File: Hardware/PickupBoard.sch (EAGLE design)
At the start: 29 parts, among them U1 TL074_

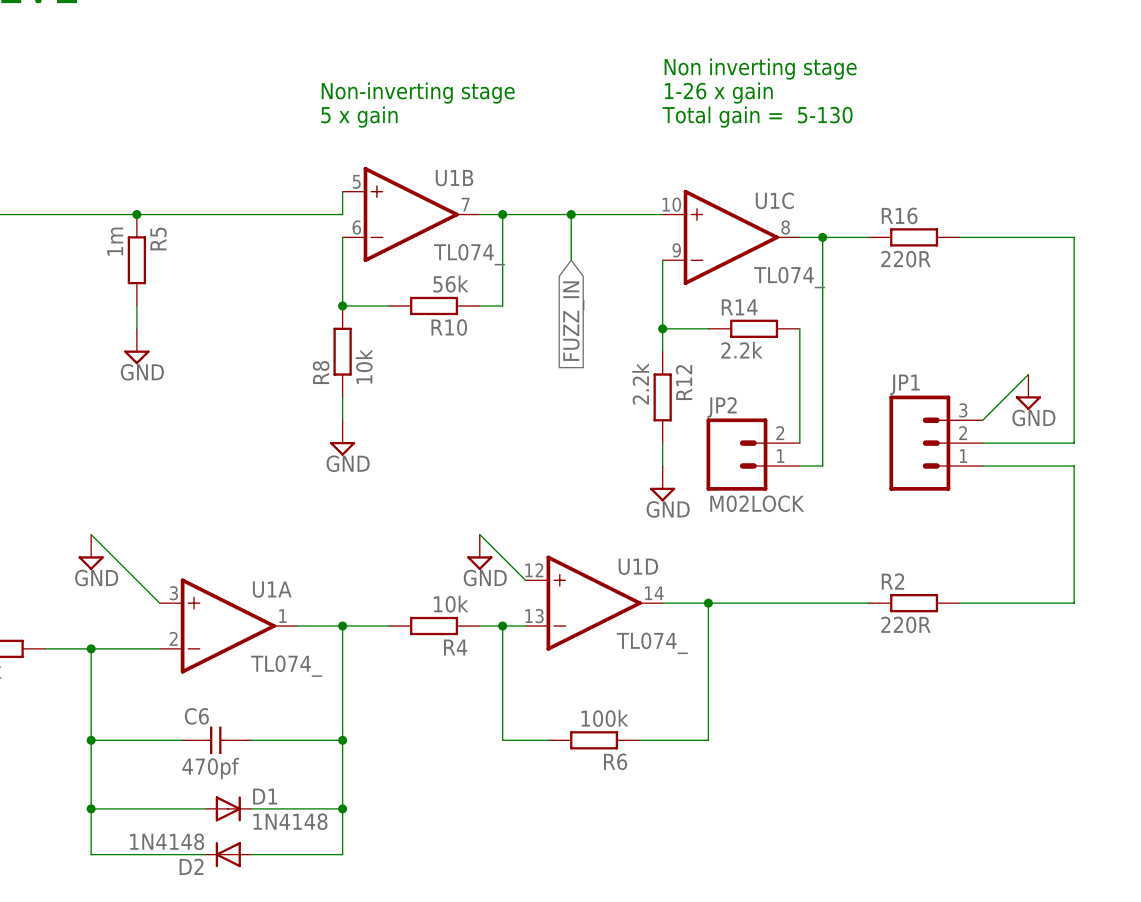
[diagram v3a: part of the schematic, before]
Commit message: Reworked layout to reduce noise / feedback
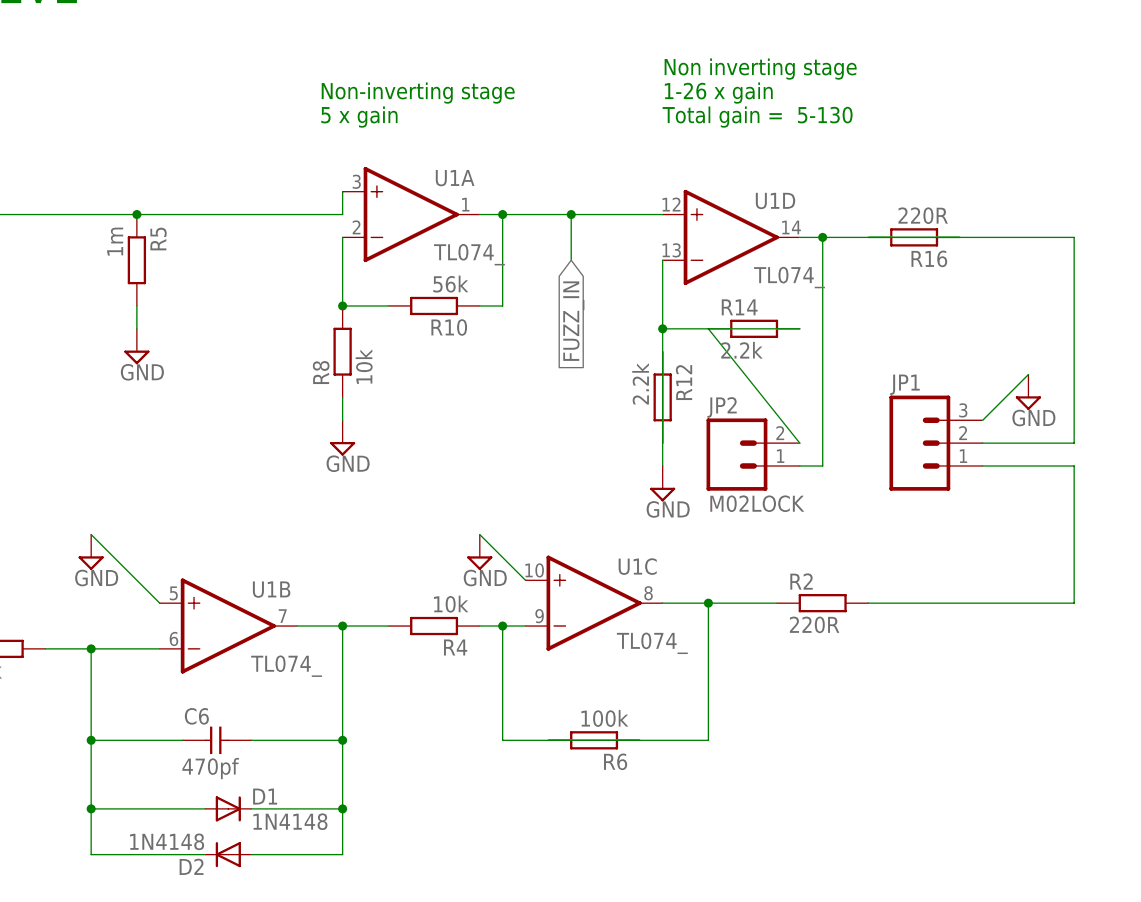
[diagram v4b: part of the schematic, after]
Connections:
- net FUZZ_IN: now also U1A.OUT, U1D.+IN; no longer U1B.OUT, U1C.+IN
- net GND: now also R12.1, U1B.+IN, U1C.+IN; no longer R12.2, U1A.+IN, U1D.+IN
- net N$1: now also U1A.+IN; no longer U1B.+IN
- net N$11: now also R6.2, U1C.OUT; no longer R6.1, U1D.OUT
- net N$2: now also U1B.OUT; no longer U1A.OUT
- net N$3: now also U1A.-IN; no longer U1B.-IN
- net N$4: now also U1B.-IN; no longer U1A.-IN
- net N$5: now also R14.1; no longer R14.2
- net N$6: now also R12.2, R14.2, U1D.-IN; no longer R12.1, R14.1, U1C.-IN
- net N$8: now also U1D.OUT; no longer U1C.OUT
- net N$9: now also R6.1, U1C.-IN; no longer R6.2, U1D.-IN
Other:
- moved on the sheet: R16, R2, U1A, U1B, U1C, U1D
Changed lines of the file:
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@@
 <?xml version="1.0" encoding="utf-8"?>
 <!DOCTYPE eagle SYSTEM "eagle.dtd">
-<eagle version="7.2.0">
+<eagle version="7.4.0">
 <drawing>
 <settings>
@@
 </plain>
 <instances>
-<instance part="U1" gate="B" x="129.54" y="127"/>
-<instance part="U1" gate="C" x="165.1" y="124.46"/>
+<instance part="U1" gate="A" x="129.54" y="127"/>
+<instance part="U1" gate="D" x="165.1" y="124.46"/>
 <instance part="R5" gate="G$1" x="99.06" y="121.92" rot="R270"/>
 <instance part="SUPPLY4" gate="GND" x="99.06" y="111.76"/>
 <instance part="R14" gate="G$1" x="167.64" y="114.3"/>
-<instance part="R16" gate="G$1" x="185.42" y="124.46"/>
+<instance part="R16" gate="G$1" x="185.42" y="124.46" rot="R180"/>
 <instance part="R8" gate="G$1" x="121.92" y="111.76" rot="R90"/>
 <instance part="R10" gate="G$1" x="132.08" y="116.84" rot="R180"/>
@@
 <instance part="FRAME1" gate="G$1" x="0" y="0"/>
 <instance part="C3" gate="G$1" x="66.04" y="78.74" rot="R270"/>
-<instance part="U1" gate="A" x="109.22" y="81.28"/>
+<instance part="U1" gate="B" x="109.22" y="81.28"/>
 <instance part="U1" gate="P" x="104.14" y="27.94"/>
-<instance part="R2" gate="G$1" x="185.42" y="83.82"/>
+<instance part="R2" gate="G$1" x="175.26" y="83.82"/>
 <instance part="U$1" gate="G$1" x="66.04" y="119.38"/>
 <instance part="U$2" gate="G$1" x="38.1" y="25.4"/>
-<instance part="U1" gate="D" x="149.86" y="83.82"/>
+<instance part="U1" gate="C" x="149.86" y="83.82"/>
 <instance part="JP1" gate="G$1" x="185.42" y="101.6"/>
 <instance part="JP2" gate="G$1" x="165.1" y="99.06"/>
@@
 </segment>
 <segment>
-<pinref part="R12" gate="G$1" pin="2"/>
+<pinref part="R12" gate="G$1" pin="1"/>
 <pinref part="SUPPLY5" gate="GND" pin="GND"/>
-<wire x1="157.48" y1="101.6" x2="157.48" y2="99.06" width="0.1524" layer="91"/>
+<wire x1="157.48" y1="111.76" x2="157.48" y2="99.06" width="0.1524" layer="91"/>
 </segment>
 <segment>
@@
 </segment>
 <segment>
-<pinref part="U1" gate="A" pin="+IN"/>
+<pinref part="U1" gate="B" pin="+IN"/>
 <pinref part="SUPPLY1" gate="GND" pin="GND"/>
 <wire x1="93.98" y1="91.44" x2="101.6" y2="83.82" width="0.1524" layer="91"/>
 </segment>
 <segment>
-<pinref part="U1" gate="D" pin="+IN"/>
+<pinref part="U1" gate="C" pin="+IN"/>
 <pinref part="SUPPLY2" gate="GND" pin="GND"/>
 <wire x1="137.16" y1="91.44" x2="142.24" y2="86.36" width="0.1524" layer="91"/>
@@
 <net name="N$8" class="0">
 <segment>
-<pinref part="U1" gate="C" pin="OUT"/>
-<wire x1="180.34" y1="124.46" x2="175.26" y2="124.46" width="0.1524" layer="91"/>
+<pinref part="U1" gate="D" pin="OUT"/>
+<wire x1="190.5" y1="124.46" x2="175.26" y2="124.46" width="0.1524" layer="91"/>
 <wire x1="175.26" y1="124.46" x2="172.72" y2="124.46" width="0.1524" layer="91"/>
 <pinref part="R16" gate="G$1" pin="1"/>
@@
 <segment>
 <pinref part="R16" gate="G$1" pin="2"/>
-<wire x1="203.2" y1="124.46" x2="190.5" y2="124.46" width="0.1524" layer="91"/>
+<wire x1="203.2" y1="124.46" x2="180.34" y2="124.46" width="0.1524" layer="91"/>
 <wire x1="203.2" y1="124.46" x2="203.2" y2="101.6" width="0.1524" layer="91"/>
 <pinref part="JP1" gate="G$1" pin="2"/>
@@
 <pinref part="R8" gate="G$1" pin="2"/>
 <wire x1="127" y1="116.84" x2="121.92" y2="116.84" width="0.1524" layer="91"/>
-<pinref part="U1" gate="B" pin="-IN"/>
+<pinref part="U1" gate="A" pin="-IN"/>
 <wire x1="121.92" y1="116.84" x2="121.92" y2="124.46" width="0.1524" layer="91"/>
 <junction x="121.92" y="116.84"/>
@@
 <net name="N$6" class="0">
 <segment>
-<pinref part="U1" gate="C" pin="-IN"/>
+<pinref part="U1" gate="D" pin="-IN"/>
 <wire x1="157.48" y1="121.92" x2="157.48" y2="114.3" width="0.1524" layer="91"/>
-<pinref part="R12" gate="G$1" pin="1"/>
-<pinref part="R14" gate="G$1" pin="1"/>
-<wire x1="157.48" y1="114.3" x2="157.48" y2="111.76" width="0.1524" layer="91"/>
-<wire x1="162.56" y1="114.3" x2="157.48" y2="114.3" width="0.1524" layer="91"/>
+<pinref part="R12" gate="G$1" pin="2"/>
+<pinref part="R14" gate="G$1" pin="2"/>
+<wire x1="157.48" y1="114.3" x2="157.48" y2="101.6" width="0.1524" layer="91"/>
+<wire x1="172.72" y1="114.3" x2="157.48" y2="114.3" width="0.1524" layer="91"/>
 <junction x="157.48" y="114.3"/>
 </segment>
@@
 <net name="N$5" class="0">
 <segment>
-<pinref part="R14" gate="G$1" pin="2"/>
-<wire x1="172.72" y1="114.3" x2="172.72" y2="101.6" width="0.1524" layer="91"/>
+<pinref part="R14" gate="G$1" pin="1"/>
+<wire x1="162.56" y1="114.3" x2="172.72" y2="101.6" width="0.1524" layer="91"/>
 <pinref part="JP2" gate="G$1" pin="2"/>
 </segment>
@@
 </segment>
 <segment>
-<pinref part="U1" gate="B" pin="OUT"/>
+<pinref part="U1" gate="A" pin="OUT"/>
 <wire x1="137.16" y1="127" x2="139.7" y2="127" width="0.1524" layer="91"/>
 <wire x1="139.7" y1="127" x2="139.7" y2="116.84" width="0.1524" layer="91"/>
@@
 <pinref part="R10" gate="G$1" pin="1"/>
 <wire x1="137.16" y1="116.84" x2="139.7" y2="116.84" width="0.1524" layer="91"/>
-<pinref part="U1" gate="C" pin="+IN"/>
+<pinref part="U1" gate="D" pin="+IN"/>
 <wire x1="139.7" y1="127" x2="147.32" y2="127" width="0.1524" layer="91"/>
 <wire x1="147.32" y1="127" x2="157.48" y2="127" width="0.1524" layer="91"/>
@@
 <wire x1="193.04" y1="99.06" x2="203.2" y2="99.06" width="0.1524" layer="91"/>
 <wire x1="203.2" y1="99.06" x2="203.2" y2="83.82" width="0.1524" layer="91"/>
-<wire x1="203.2" y1="83.82" x2="190.5" y2="83.82" width="0.1524" layer="91"/>
+<wire x1="203.2" y1="83.82" x2="180.34" y2="83.82" width="0.1524" layer="91"/>
 </segment>
 </net>
@@
 <pinref part="R5" gate="G$1" pin="1"/>
 <wire x1="58.42" y1="127" x2="99.06" y2="127" width="0.1524" layer="91"/>
-<pinref part="U1" gate="B" pin="+IN"/>
+<pinref part="U1" gate="A" pin="+IN"/>
 <wire x1="99.06" y1="127" x2="121.92" y2="127" width="0.1524" layer="91"/>
 <wire x1="121.92" y1="127" x2="121.92" y2="129.54" width="0.1524" layer="91"/>
@@
 <net name="N$4" class="0">
 <segment>
-<pinref part="U1" gate="A" pin="-IN"/>
+<pinref part="U1" gate="B" pin="-IN"/>
 <pinref part="R1" gate="G$1" pin="2"/>
 <wire x1="88.9" y1="78.74" x2="93.98" y2="78.74" width="0.1524" layer="91"/>
@@
 <net name="N$2" class="0">
 <segment>
-<pinref part="U1" gate="A" pin="OUT"/>
+<pinref part="U1" gate="B" pin="OUT"/>
 <wire x1="116.84" y1="81.28" x2="121.92" y2="81.28" width="0.1524" layer="91"/>
 <pinref part="D1" gate="G$1" pin="C"/>
@@
 <segment>
 <pinref part="R4" gate="G$1" pin="1"/>
-<pinref part="U1" gate="D" pin="-IN"/>
+<pinref part="U1" gate="C" pin="-IN"/>
 <wire x1="142.24" y1="81.28" x2="139.7" y2="81.28" width="0.1524" layer="91"/>
-<pinref part="R6" gate="G$1" pin="2"/>
+<pinref part="R6" gate="G$1" pin="1"/>
 <wire x1="139.7" y1="81.28" x2="137.16" y2="81.28" width="0.1524" layer="91"/>
-<wire x1="144.78" y1="68.58" x2="139.7" y2="68.58" width="0.1524" layer="91"/>
+<wire x1="154.94" y1="68.58" x2="139.7" y2="68.58" width="0.1524" layer="91"/>
 <wire x1="139.7" y1="68.58" x2="139.7" y2="81.28" width="0.1524" layer="91"/>
 <junction x="139.7" y="81.28"/>
@@
 <net name="N$11" class="0">
 <segment>
-<pinref part="U1" gate="D" pin="OUT"/>
+<pinref part="U1" gate="C" pin="OUT"/>
 <pinref part="R2" gate="G$1" pin="1"/>
-<wire x1="180.34" y1="83.82" x2="162.56" y2="83.82" width="0.1524" layer="91"/>
-<pinref part="R6" gate="G$1" pin="1"/>
+<wire x1="170.18" y1="83.82" x2="162.56" y2="83.82" width="0.1524" layer="91"/>
+<pinref part="R6" gate="G$1" pin="2"/>
 <wire x1="162.56" y1="83.82" x2="157.48" y2="83.82" width="0.1524" layer="91"/>
-<wire x1="154.94" y1="68.58" x2="162.56" y2="68.58" width="0.1524" layer="91"/>
+<wire x1="144.78" y1="68.58" x2="162.56" y2="68.58" width="0.1524" layer="91"/>
 <wire x1="162.56" y1="68.58" x2="162.56" y2="83.82" width="0.1524" layer="91"/>
 <junction x="162.56" y="83.82"/>

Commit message: Rev 4 pcb
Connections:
- net N$2: now also C6.2; no longer C6.1
- net N$4: now also C6.1; no longer C6.2
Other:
- moved on the sheet: C6, R12, R14, R16, R6
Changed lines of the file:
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@@
 <?xml version="1.0" encoding="utf-8"?>
 <!DOCTYPE eagle SYSTEM "eagle.dtd">
-<eagle version="7.4.0">
+<eagle version="7.2.0">
 <drawing>
 <settings>
@@
 <instance part="R5" gate="G$1" x="99.06" y="121.92" rot="R270"/>
 <instance part="SUPPLY4" gate="GND" x="99.06" y="111.76"/>
-<instance part="R14" gate="G$1" x="167.64" y="114.3"/>
-<instance part="R16" gate="G$1" x="185.42" y="124.46" rot="R180"/>
+<instance part="R14" gate="G$1" x="167.64" y="114.3" rot="R180"/>
+<instance part="R16" gate="G$1" x="185.42" y="124.46"/>
 <instance part="R8" gate="G$1" x="121.92" y="111.76" rot="R90"/>
 <instance part="R10" gate="G$1" x="132.08" y="116.84" rot="R180"/>
 <instance part="SUPPLY9" gate="GND" x="121.92" y="101.6"/>
-<instance part="R12" gate="G$1" x="157.48" y="106.68" rot="R270"/>
+<instance part="R12" gate="G$1" x="157.48" y="106.68" rot="R90"/>
 <instance part="SUPPLY5" gate="GND" x="157.48" y="96.52"/>
 <instance part="GND21" gate="1" x="76.2" y="27.94"/>
@@
 <instance part="D1" gate="G$1" x="109.22" y="60.96"/>
 <instance part="D2" gate="G$1" x="109.22" y="55.88" rot="R180"/>
-<instance part="C6" gate="G$1" x="109.22" y="68.58" rot="R270"/>
+<instance part="C6" gate="G$1" x="109.22" y="68.58" rot="R90"/>
 <instance part="R4" gate="G$1" x="132.08" y="81.28" rot="R180"/>
 <instance part="SUPPLY2" gate="GND" x="137.16" y="88.9"/>
-<instance part="R6" gate="G$1" x="149.86" y="68.58" rot="R180"/>
+<instance part="R6" gate="G$1" x="149.86" y="68.58"/>
 </instances>
 <busses>
@@
 <pinref part="R12" gate="G$1" pin="1"/>
 <pinref part="SUPPLY5" gate="GND" pin="GND"/>
-<wire x1="157.48" y1="111.76" x2="157.48" y2="99.06" width="0.1524" layer="91"/>
+<wire x1="157.48" y1="101.6" x2="157.48" y2="99.06" width="0.1524" layer="91"/>
 </segment>
 <segment>
@@
 <segment>
 <pinref part="U1" gate="D" pin="OUT"/>
-<wire x1="190.5" y1="124.46" x2="175.26" y2="124.46" width="0.1524" layer="91"/>
+<wire x1="180.34" y1="124.46" x2="175.26" y2="124.46" width="0.1524" layer="91"/>
 <wire x1="175.26" y1="124.46" x2="172.72" y2="124.46" width="0.1524" layer="91"/>
 <pinref part="R16" gate="G$1" pin="1"/>
@@
 <segment>
 <pinref part="R16" gate="G$1" pin="2"/>
-<wire x1="203.2" y1="124.46" x2="180.34" y2="124.46" width="0.1524" layer="91"/>
+<wire x1="203.2" y1="124.46" x2="190.5" y2="124.46" width="0.1524" layer="91"/>
 <wire x1="203.2" y1="124.46" x2="203.2" y2="101.6" width="0.1524" layer="91"/>
 <pinref part="JP1" gate="G$1" pin="2"/>
@@
 <pinref part="R12" gate="G$1" pin="2"/>
 <pinref part="R14" gate="G$1" pin="2"/>
-<wire x1="157.48" y1="114.3" x2="157.48" y2="101.6" width="0.1524" layer="91"/>
-<wire x1="172.72" y1="114.3" x2="157.48" y2="114.3" width="0.1524" layer="91"/>
+<wire x1="157.48" y1="114.3" x2="157.48" y2="111.76" width="0.1524" layer="91"/>
+<wire x1="162.56" y1="114.3" x2="157.48" y2="114.3" width="0.1524" layer="91"/>
 <junction x="157.48" y="114.3"/>
 </segment>
@@
 <segment>
 <pinref part="R14" gate="G$1" pin="1"/>
-<wire x1="162.56" y1="114.3" x2="172.72" y2="101.6" width="0.1524" layer="91"/>
+<wire x1="172.72" y1="114.3" x2="172.72" y2="101.6" width="0.1524" layer="91"/>
 <pinref part="JP2" gate="G$1" pin="2"/>
 </segment>
@@
 <wire x1="93.98" y1="55.88" x2="93.98" y2="60.96" width="0.1524" layer="91"/>
 <junction x="93.98" y="60.96"/>
-<pinref part="C6" gate="G$1" pin="2"/>
-<wire x1="104.14" y1="68.58" x2="93.98" y2="68.58" width="0.1524" layer="91"/>
+<pinref part="C6" gate="G$1" pin="1"/>
+<wire x1="106.68" y1="68.58" x2="93.98" y2="68.58" width="0.1524" layer="91"/>
 <junction x="93.98" y="68.58"/>
 </segment>
@@
 <wire x1="121.92" y1="55.88" x2="121.92" y2="60.96" width="0.1524" layer="91"/>
 <junction x="121.92" y="60.96"/>
-<pinref part="C6" gate="G$1" pin="1"/>
-<wire x1="111.76" y1="68.58" x2="121.92" y2="68.58" width="0.1524" layer="91"/>
+<pinref part="C6" gate="G$1" pin="2"/>
+<wire x1="114.3" y1="68.58" x2="121.92" y2="68.58" width="0.1524" layer="91"/>
 <junction x="121.92" y="68.58"/>
 <pinref part="R4" gate="G$1" pin="2"/>
@@
 <pinref part="R6" gate="G$1" pin="1"/>
 <wire x1="139.7" y1="81.28" x2="137.16" y2="81.28" width="0.1524" layer="91"/>
-<wire x1="154.94" y1="68.58" x2="139.7" y2="68.58" width="0.1524" layer="91"/>
+<wire x1="144.78" y1="68.58" x2="139.7" y2="68.58" width="0.1524" layer="91"/>
 <wire x1="139.7" y1="68.58" x2="139.7" y2="81.28" width="0.1524" layer="91"/>
 <junction x="139.7" y="81.28"/>
@@
 <pinref part="R6" gate="G$1" pin="2"/>
 <wire x1="162.56" y1="83.82" x2="157.48" y2="83.82" width="0.1524" layer="91"/>
-<wire x1="144.78" y1="68.58" x2="162.56" y2="68.58" width="0.1524" layer="91"/>
+<wire x1="154.94" y1="68.58" x2="162.56" y2="68.58" width="0.1524" layer="91"/>
 <wire x1="162.56" y1="68.58" x2="162.56" y2="83.82" width="0.1524" layer="91"/>
 <junction x="162.56" y="83.82"/>

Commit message: First rev5 upload
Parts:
- removed D1: 1N4148, MusicThingModular:SMALL_DIODEDO35-7
- removed R14: 2.2k, MusicThingModular:RESISTOR7MM
- removed R16: 220R, MusicThingModular:RESISTOR7MM
- removed U1: TL074_, MusicThingModular:TL074_
- added C7: 330pf, we-rcl:CAPACITOR-0603
- added D3: 1N914.3, gm-diodes:1N914.3
- added R13: 200R, MusicThingModular:RESISTOR7MM
- added R7: 10K, MusicThingModular:RESISTOR7MM
- added R9: 32k, MusicThingModular:RESISTOR7MM
- added U2: TL074_, MusicThingModular:TL074_
- C3: value 470n -> 47n; device TomW:C-EU050-024X044 -> we-rcl:CAPACITOR-0603
- C6: value 470pf -> 330pf; device TomW:C-EU050-024X044 -> we-rcl:CAPACITOR-0603
- D2: value 1N4148 -> 1N914.3; device MusicThingModular:SMALL_DIODEDO35-7 -> gm-diodes:1N914.3
- JP1: value (none) -> INOUT
- JP2: value M02LOCK -> POT
- R1: value 10k -> 1m
- R10: value 56k -> 200R
- R12: value 2.2k -> 10K
- R2: value 220R -> 10k
- R5: value 1m -> 10k
- R6: value 100k -> 10K
- R8: value 10k -> 150k
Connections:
- removed net FUZZ_IN: C3.2, R10.1, U1A.OUT, U1D.+IN
- removed net N$1: R5.1, U$1.3, U1A.+IN
- removed net N$10: JP1.2, R16.2
- removed net N$5: JP2.2, R14.1
- new net GAIN_IN: R1.2, R2.2, U$1.3
- new net N$12: C7.2, R8.1, U2C.OUT
- new net N$15: C6.2, R10.2, R12.1, R5.1, U2A.OUT
- new net N$16: JP1.2, R10.1
- new net N$17: R12.2, U2B.+IN
- new net N$18: R6.2, U2B.-IN, U2B.OUT
- new net N$19: JP1.1, R13.1
- net +12V: now also U2P.V+; no longer U1P.V+
- net -12V: now also U2P.V-; no longer U1P.V-
- net GND: now also D2.A, D3.C, R1.1, R4.1, R9.1, U2D.+IN; no longer R12.1, R5.2, R8.1, U1B.+IN, U1C.+IN
- net N$11: now also C7.1, R8.2, R9.2, U2C.-IN; no longer R2.1, R6.2, U1C.OUT
- net N$13: now also R13.2; no longer JP1.1, R2.2
- net N$2: now also R2.1, U2A.+IN; no longer C6.2, D1.C, D2.A, R4.2, U1B.OUT
- net N$3: now also U2D.-IN, U2D.OUT; no longer R10.2, R8.2, U1A.-IN
- net N$4: now also C3.2, JP2.2, U2A.-IN; no longer D1.A, D2.C, R1.2, U1B.-IN
- net N$6: now also JP2.1, R5.2; no longer R12.2, R14.2, U1D.-IN
- net N$7: now also R4.2; no longer R1.1
- net N$8: now also R7.1, U2C.+IN; no longer JP2.1, R16.1, U1D.OUT
- net N$9: now also D2.C, D3.A, R7.2; no longer R4.1, U1C.-IN
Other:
- note added: "C2 at 47n cleans up guitar input by cutting bass remove or switch for full-range input"
- note added: "Gain: 1x - 100x Original corner freq = 1064hz high pass (2.2k + 68n) 10k + 47n = 338hz high pass"
- note added: "Gain: 5.6x to make up for diode clipping"
- note removed: "Non inverting stage 1-26 x gain Total gain = 5-130"
- note removed: "Non-inverting stage 5 x gain"
- moved on the sheet: D2, JP1, JP2, R1, R10, R12, R2, R4, R5, R6, R8
